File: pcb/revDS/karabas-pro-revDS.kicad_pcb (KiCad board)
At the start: 2 copper layers, 101.6 x 147.3 mm, 215 parts, among them CON1 CF-CARD, CON2 SD, CON3 VGA, CON4 Joystick, CON5 Keyboard, CON6 Mouse, CON7 Audio, CON8 12V, CON9 MicroSD', J1 Floppy, J10 Ext Joystick, J2 FPGA JTAG, J3 Floppy, J4 uBus, J5 AVR JTAG, J6 AVR UART, J7 ESP-BUS, J8 Tape In, J9 Tape Out, Q1 BC856, Q2 BC548, SW1 SW_Push, SW2 SW_Push, SW4 SW_SPST, U1 EP4CE10E22C8N, U10 ESP-12E, U11 TDA1543, U12 AMS1117-3.3, U13 AMS1117-2.5, U14 AMS1117-1.2, U15 LM2596S-5, U16 LM311, U17 74LS06, U18 74LS38, U2 CY62167EV30LL, U3 W25Q16, U3''1 W25Q16, U4 EPM3128ATC100-10N, U5 ATMEGA328-AU, U6 MB8877A, U7 TXB0104PW, U8 TXB0104PW, U9 DS1307Z+, X1 SG-7050CAN, Y1 32768Hz, Y2 16MHz

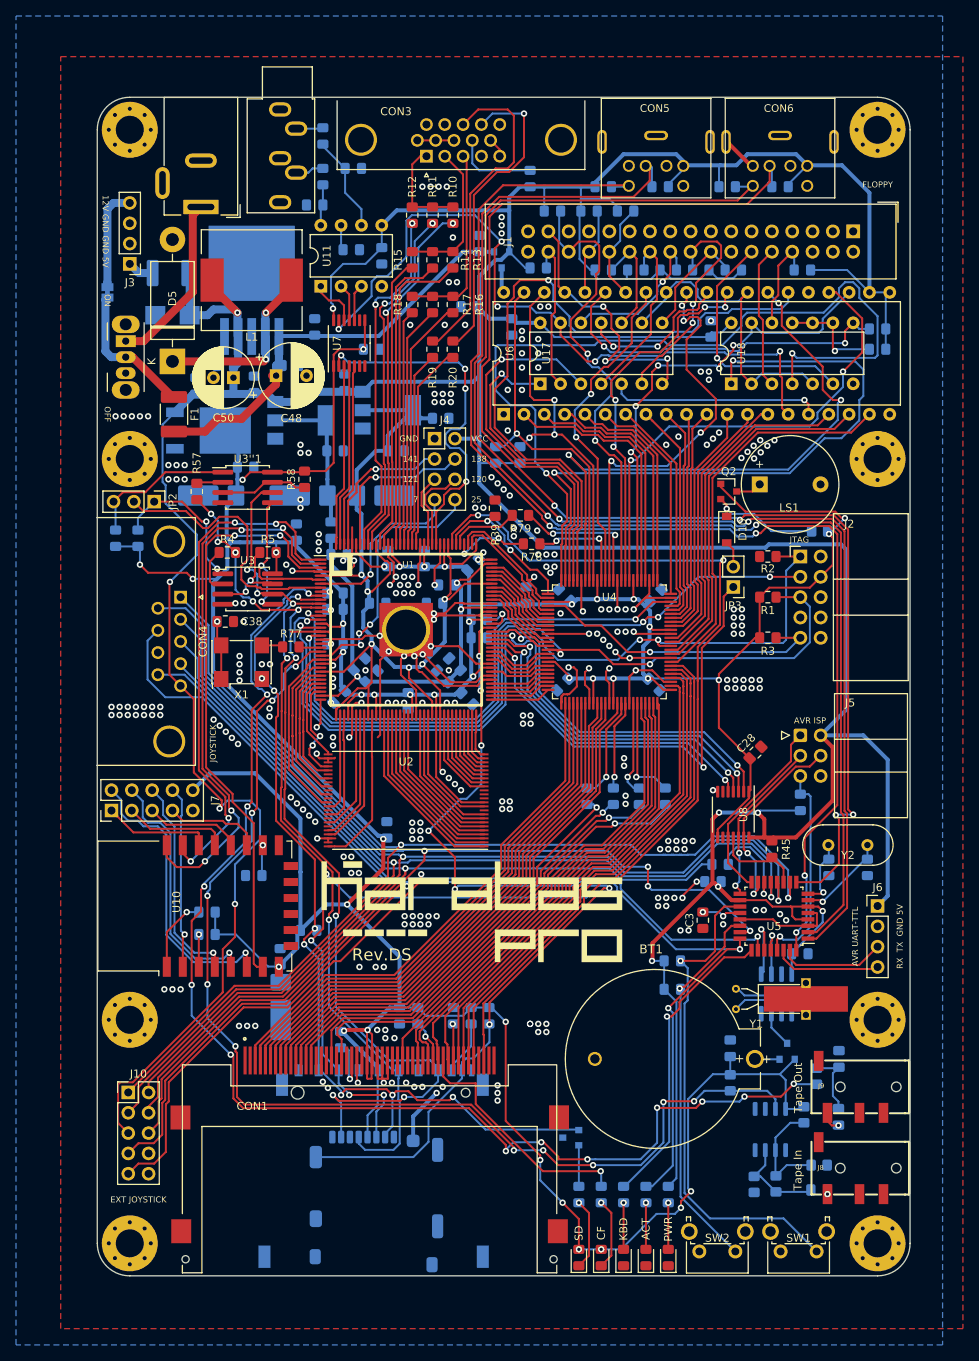
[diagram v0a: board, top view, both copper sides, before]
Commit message: Multi target ep4ec6, ep4ce10, ep3c10 (#53)
* Moved syn files to ep4ce6 subfolder

* fixed abs path

* fixed abs path

* Project file for ep4ce10 target

* new build dir structure

* added ep4ce10 build dir

* updated readme

* Builds for multiple targets: ep4ce6, ep4ce10

* removed outdated builds

* ep3c10 target

* Added ep3c10 build

* Added ep3c10 target, added tape in, out, buzzer out

* Extended CF footprint
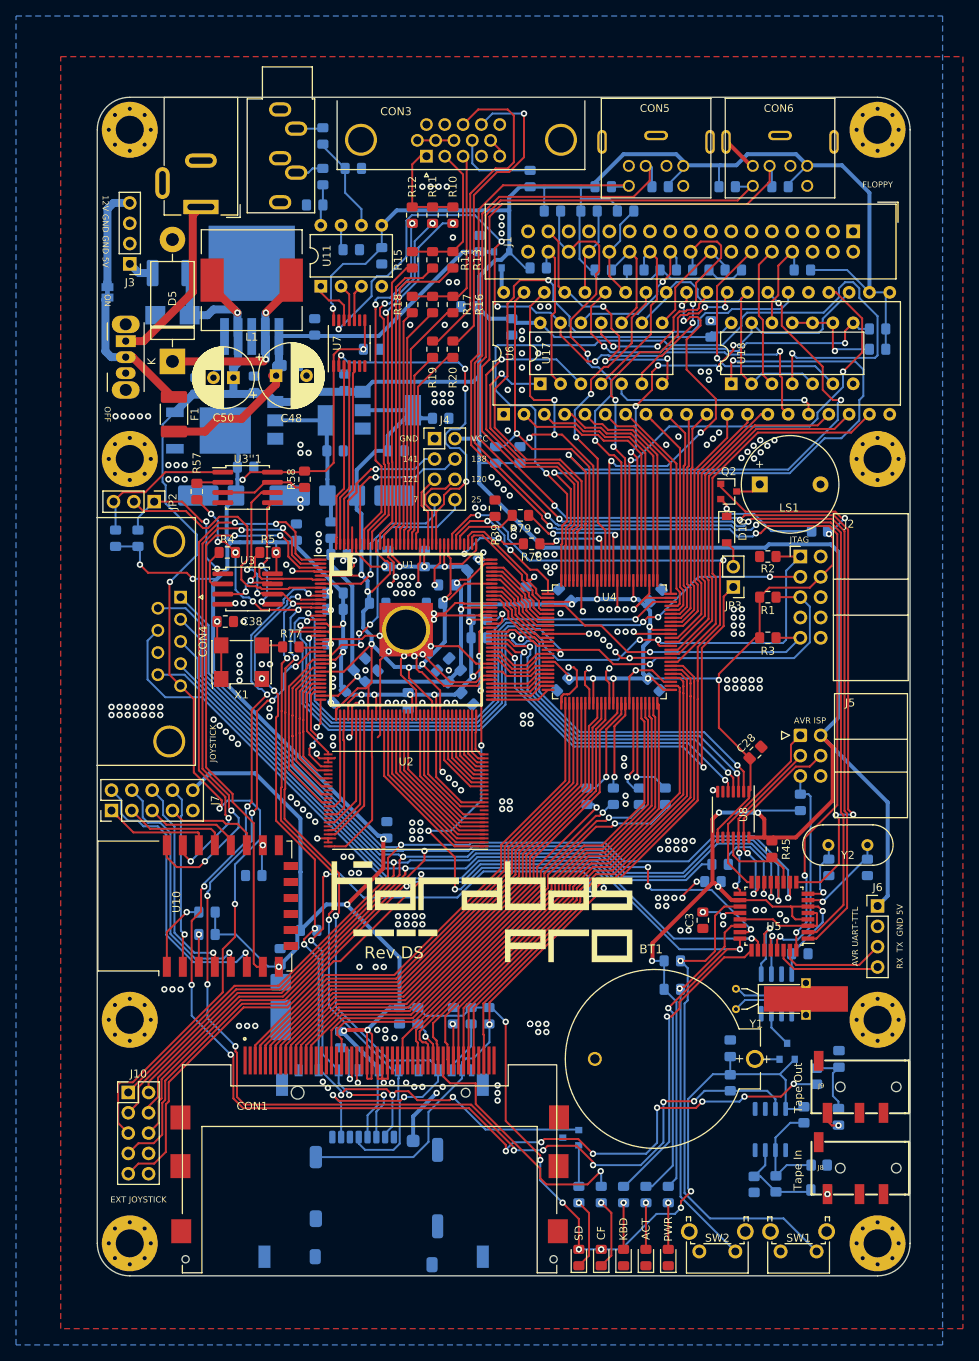
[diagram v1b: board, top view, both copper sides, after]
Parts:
- removed the G*** at (154.7, 119.1)
- added G***: LOGO, footprints:karabas_pro_logo4_copper, B.Cu at (152.4, 131.8)
- moved G*** 1.27 mm to (147.3, 127.0)
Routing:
- net VCC: track 650.9 -> 646.2 mm
- net /SD_DI: track 163.4 -> 166.8 mm
- net /~SD_DET: track 115.1 -> 117.5 mm
- net /LED_BUSY: track 30.0 -> 32.1 mm
- net /LED2: track 185.6 -> 187.2 mm
- net /JOY_R2: track 125.6 -> 126.8 mm
- net /JOY_FIRE2: track 148.9 -> 149.7 mm
- net /JOY_UP: track 149.7 -> 150.5 mm
- net /JOY_LEFT: track 144.7 -> 145.5 mm
- net /JOY_DOWN: track 146.2 -> 146.9 mm
- net TAPE_IN: track 144.0 -> 144.7 mm
- net /JOY_FIRE1: track 149.8 -> 150.5 mm
- net /I2C_SDA: track 8.61 -> 9.18 mm
- net GND: vias 294 -> 293

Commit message: Fixed beeper
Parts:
- Q2: value BC548 -> BC847
- R48: value 1k -> 15k
- moved Q2 1.03 mm to (177.8, 73.7), turned to 90 degrees
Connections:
- CON1 pad 24: Net-(CON1-Pad24) -> (no net)
- CON1 pad 25: Net-(CON1-Pad25) -> (no net)
- CON1 pad 26: Net-(CON1-Pad26) -> (no net)
- CON1 pad 33: Net-(CON1-Pad33) -> (no net)
- CON1 pad 37: Net-(CON1-Pad37) -> (no net)
- CON1 pad 40: Net-(CON1-Pad40) -> (no net)
- CON1 pad 42: Net-(CON1-Pad42) -> (no net)
- CON1 pad 43: Net-(CON1-Pad43) -> (no net)
- CON2 pad 11: Net-(CON2-Pad11) -> (no net)
- CON2 pad 9: Net-(CON2-Pad9) -> (no net)
- CON3 pad 11: Net-(CON3-Pad11) -> (no net)
- CON3 pad 12: Net-(CON3-Pad12) -> (no net)
- CON3 pad 15: Net-(CON3-Pad15) -> (no net)
- CON3 pad 4: Net-(CON3-Pad4) -> (no net)
- CON5 pad 2: Net-(CON5-Pad2) -> (no net)
- CON5 pad 6: Net-(CON5-Pad6) -> (no net)
- CON6 pad 2: Net-(CON6-Pad2) -> (no net)
- CON6 pad 6: Net-(CON6-Pad6) -> (no net)
- J1 pad 14: Net-(J1-Pad14) -> (no net)
- J1 pad 2: Net-(J1-Pad2) -> (no net)
- J1 pad 34: Net-(J1-Pad34) -> (no net)
- J1 pad 4: Net-(J1-Pad4) -> (no net)
- J1 pad 6: Net-(J1-Pad6) -> (no net)
- J10 pad 10: Net-(J10-Pad10) -> (no net)
- J2 pad 6: Net-(J2-Pad6) -> (no net)
- J2 pad 7: Net-(J2-Pad7) -> (no net)
- J2 pad 8: Net-(J2-Pad8) -> (no net)
- J8 pad R1: Net-(J8-PadR1) -> (no net)
- J9 pad R1: Net-(J9-PadR1) -> (no net)
- Q2 pad 1: VCC3_3 -> Net-(D10-Pad1)
- Q2 pad 2: Net-(D10-Pad1) -> Net-(LS1-Pad1)
- Q2 pad 3: Net-(LS1-Pad1) -> VCC3_3
- U10 pad 10: Net-(U10-Pad10) -> (no net)
- U10 pad 11: Net-(U10-Pad11) -> (no net)
- U10 pad 12: Net-(U10-Pad12) -> (no net)
- U10 pad 13: Net-(U10-Pad13) -> (no net)
- U10 pad 14: Net-(U10-Pad14) -> (no net)
- U10 pad 9: Net-(U10-Pad9) -> (no net)
- U16 pad 5: Net-(U16-Pad5) -> (no net)
- U16 pad 6: Net-(U16-Pad6) -> (no net)
- U2 pad 10: Net-(U2-Pad10) -> (no net)
- U2 pad 13: Net-(U2-Pad13) -> (no net)
- U2 pad 14: Net-(U2-Pad14) -> (no net)
- U2 pad 15: Net-(U2-Pad15) -> (no net)
- U2 pad 30: Net-(U2-Pad30) -> (no net)
- U2 pad 32: Net-(U2-Pad32) -> (no net)
- U2 pad 34: Net-(U2-Pad34) -> (no net)
- U2 pad 36: Net-(U2-Pad36) -> (no net)
- U2 pad 39: Net-(U2-Pad39) -> (no net)
- U2 pad 41: Net-(U2-Pad41) -> (no net)
- U2 pad 43: Net-(U2-Pad43) -> (no net)
- U6 pad 25: Net-(U6-Pad25) -> (no net)
- U7 pad 6: Net-(U7-Pad6) -> (no net)
- U7 pad 9: Net-(U7-Pad9) -> (no net)
- U8 pad 6: Net-(U8-Pad6) -> (no net)
- U8 pad 9: Net-(U8-Pad9) -> (no net)
- U9 pad 7: Net-(U9-Pad7) -> (no net)
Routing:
- net Net-(LS1-Pad1): track 3.75 -> 5.24 mm
- net VCC3_3: track 642.5 -> 643.7 mm
- net Net-(D10-Pad1): track 14.2 -> 15.3 mm

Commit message: Updated gerbers, schematics for revDS
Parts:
- R48: value 15k -> 15k*
- R80: value 10k -> 5k1
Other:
- board text added: "Rev.DS'"
- board text added: "Special thanks to: solegstar, tank-uk, nihirash, dr_max, xdemox, kalantaj"
- board text removed: "Rev.DS"
- board text removed: "Special thanks to: solegstar, tank-uk, nihirash, dr_max, tslabs, kalantaj"
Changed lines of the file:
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@@
     (add_net "Net-(C56-Pad1)")
     (add_net "Net-(C56-Pad2)")
-    (add_net "Net-(CON1-Pad24)")
-    (add_net "Net-(CON1-Pad25)")
-    (add_net "Net-(CON1-Pad26)")
-    (add_net "Net-(CON1-Pad33)")
     (add_net "Net-(CON1-Pad36)")
-    (add_net "Net-(CON1-Pad37)")
-    (add_net "Net-(CON1-Pad40)")
-    (add_net "Net-(CON1-Pad42)")
-    (add_net "Net-(CON1-Pad43)")
     (add_net "Net-(CON1-Pad44)")
     (add_net "Net-(CON1-Pad46)")
-    (add_net "Net-(CON2-Pad11)")
     (add_net "Net-(CON2-Pad8)")
-    (add_net "Net-(CON2-Pad9)")
-    (add_net "Net-(CON3-Pad11)")
-    (add_net "Net-(CON3-Pad12)")
-    (add_net "Net-(CON3-Pad15)")
-    (add_net "Net-(CON3-Pad4)")
     (add_net "Net-(CON3-Pad9)")
-    (add_net "Net-(CON5-Pad6)")
-    (add_net "Net-(CON6-Pad2)")
-    (add_net "Net-(CON6-Pad6)")
     (add_net "Net-(CON8-Pad1)")
     (add_net "Net-(D10-Pad1)")
@@
     (add_net "Net-(F1-Pad1)")
     (add_net "Net-(F2-Pad1)")
-    (add_net "Net-(J1-Pad14)")
-    (add_net "Net-(J1-Pad2)")
-    (add_net "Net-(J1-Pad34)")
-    (add_net "Net-(J1-Pad4)")
-    (add_net "Net-(J1-Pad6)")
-    (add_net "Net-(J10-Pad10)")
-    (add_net "Net-(J2-Pad6)")
-    (add_net "Net-(J2-Pad7)")
-    (add_net "Net-(J2-Pad8)")
     (add_net "Net-(J3-Pad4)")
-    (add_net "Net-(J8-PadR1)")
-    (add_net "Net-(J9-PadR1)")
     (add_net "Net-(LS1-Pad1)")
     (add_net "Net-(Q1-Pad2)")
@@
     (add_net "Net-(R79-Pad1)")
     (add_net "Net-(R80-Pad2)")
-    (add_net "Net-(U10-Pad10)")
-    (add_net "Net-(U10-Pad11)")
-    (add_net "Net-(U10-Pad12)")
-    (add_net "Net-(U10-Pad13)")
-    (add_net "Net-(U10-Pad14)")
-    (add_net "Net-(U10-Pad9)")
-    (add_net "Net-(U16-Pad5)")
-    (add_net "Net-(U16-Pad6)")
-    (add_net "Net-(U2-Pad10)")
-    (add_net "Net-(U2-Pad13)")
-    (add_net "Net-(U2-Pad14)")
-    (add_net "Net-(U2-Pad15)")
-    (add_net "Net-(U2-Pad30)")
-    (add_net "Net-(U2-Pad32)")
-    (add_net "Net-(U2-Pad34)")
-    (add_net "Net-(U2-Pad36)")
-    (add_net "Net-(U2-Pad39)")
-    (add_net "Net-(U2-Pad41)")
-    (add_net "Net-(U2-Pad43)")
-    (add_net "Net-(U6-Pad25)")
-    (add_net "Net-(U7-Pad6)")
-    (add_net "Net-(U7-Pad9)")
-    (add_net "Net-(U8-Pad6)")
-    (add_net "Net-(U8-Pad9)")
     (add_net "Net-(U9-Pad1)")
     (add_net "Net-(U9-Pad2)")
-    (add_net "Net-(U9-Pad7)")
     (add_net TAPE_IN)
     (add_net TAPE_OUT)
@@
       (effects (font (size 1 1) (thickness 0.15)) (justify mirror))
     )
-    (fp_text value 15k (at 0 -1.65) (layer B.Fab)
+    (fp_text value 15k* (at 0 -1.65) (layer B.Fab)
       (effects (font (size 1 1) (thickness 0.15)) (justify mirror))
     )
@@
       (effects (font (size 1 1) (thickness 0.15)) (justify mirror))
     )
-    (fp_text value 10k (at 0 -1.65 90) (layer B.Fab)
+    (fp_text value 5k1 (at 0 -1.65 90) (layer B.Fab)
       (effects (font (size 1 1) (thickness 0.15)) (justify mirror))
     )
@@
     )
   )
-  (gr_text "Rev.DS\n" (at 136.144 132.334) (layer F.SilkS)
+  (gr_text "Rev.DS'\n" (at 136.144 132.334) (layer F.SilkS)
     (effects (font (size 1.5 1.5) (thickness 0.3)))
   )
-  (gr_text "Rev.DS\n" (at 161.544 134.366) (layer B.Mask)
+  (gr_text "Rev.DS'\n" (at 161.544 134.366) (layer B.Mask)
     (effects (font (size 1.5 1.5) (thickness 0.3)) (justify mirror))
   )
@@
     (effects (font (size 1.5 1.5) (thickness 0.3)) (justify left mirror))
   )
-  (gr_text "Special thanks to:\nsolegstar, tank-uk, nihirash, \ndr_max, tslabs, kalantaj" (at 196.088 94.488 90) (layer B.Mask)
+  (gr_text "Special thanks to:\nsolegstar, tank-uk, nihirash, \ndr_max, xdemox, kalantaj" (at 196.088 94.488 90) (layer B.Mask)
     (effects (font (size 1.5 1.5) (thickness 0.3)) (justify mirror))
   )

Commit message: Updated logo
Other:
- board text added: "Rev.DS"
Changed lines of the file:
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@@
     (effects (font (size 1.5 1.5) (thickness 0.3)))
   )
-  (gr_text "Rev.DS'\n" (at 161.544 134.366) (layer B.Mask)
+  (gr_text "Rev.DS\n" (at 161.544 134.366) (layer B.Mask)
     (effects (font (size 1.5 1.5) (thickness 0.3)) (justify mirror))
   )
